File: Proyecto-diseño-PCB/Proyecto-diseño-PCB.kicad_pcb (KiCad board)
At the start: 4 copper layers, 41 parts, among them J1 USB_B_Micro, J2 PROGRAMACIÓN/DEPURACIÓN, J3 LADO A, J4 LADO B, SW1 BOTON, SW2 BOTON, SW3 RESET, U1 TPD2EUSB30, U2 LP2950-3.3_TO252, U3 PIC18LF45K50-I/P

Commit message: rest of the f-ing owl
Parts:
- C1, C2, C3: footprint Capacitor_THT:C_Disc_D3.4mm_W2.1mm_P2.50mm -> Capacitor_SMD:C_1206_3216Metric_Pad1.33x1.80mm_HandSolder
- C4, C5, C6, C7, C8: footprint Capacitor_THT:C_Disc_D3.4mm_W2.1mm_P2.50mm -> Capacitor_SMD:C_1206_3216Metric_Pad1.33x1.80mm_HandSolder; moved to B.Cu
- J3: footprint Connector_PinSocket_2.54mm:PinSocket_1x15_P2.54mm_Vertical -> Connector_PinSocket_2.54mm:PinSocket_1x16_P2.54mm_Vertical
- J4: footprint Connector_PinSocket_2.54mm:PinSocket_1x16_P2.54mm_Vertical -> Connector_PinSocket_2.54mm:PinSocket_1x14_P2.54mm_Vertical
- R1, R3: footprint Resistor_THT:R_Axial_DIN0204_L3.6mm_D1.6mm_P5.08mm_Horizontal -> Resistor_SMD:R_1206_3216Metric_Pad1.30x1.75mm_HandSolder; moved to B.Cu
- R10, R11, R12, R13, R2, R4, R5, R6, R7, R8, R9: footprint Resistor_THT:R_Axial_DIN0204_L3.6mm_D1.6mm_P5.08mm_Horizontal -> Resistor_SMD:R_1206_3216Metric_Pad1.30x1.75mm_HandSolder
- U1: moved to B.Cu
- moved R12 239.8 mm to (181.2, 73.7), turned to -90 degrees
- moved D5 237.8 mm to (169.8, 67.8)
- moved R11 235.6 mm to (177.9, 73.7), turned to -90 degrees
- moved D4 231.4 mm to (164.7, 67.8)
- moved R7 230.8 mm to (180.4, 83.6), turned to 180 degrees
- moved R5 227.9 mm to (180.5, 89.2), turned to 180 degrees
- moved R3 224.2 mm to (175.7, 78.7)
- moved R1 222.1 mm to (175.7, 81.7)
- moved C2 214.2 mm to (180.4, 86.4)
- moved R4 212.9 mm to (166.5, 92.3), turned to 90 degrees
- moved U1 207.1 mm to (171.3, 80.2), turned to 90 degrees
- moved R6 206.2 mm to (158.1, 92.3), turned to 90 degrees
- moved C8 205.6 mm to (167.3, 91.9), turned to 90 degrees
- moved D1 196.8 mm to (176.9, 88.4), turned to 90 degrees
- moved C1 194.4 mm to (162.2, 92.4), turned to -90 degrees
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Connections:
- net Net-(FL1-CB) renamed /VI
- J3 pad 10: /RA5 -> /RE0
- J3 pad 11: /RA4 -> /RA5
- J3 pad 12: /RA3 -> /RA4
- J3 pad 13: /RA2 -> /RA3
- J3 pad 14: /RA1 -> /RA2
- J3 pad 15: /RA0 -> /RA1
- U3 pad 19: /LED_ROJO -> /BOTON1
- U3 pad 20: /LED_VERDE -> /BOTON2
- U3 pad 21: /BOTON2 -> /LED_VERDE
- U3 pad 22: /BOTON1 -> /LED_ROJO
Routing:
- net 5V: track 0.00 -> 52.5 mm, vias 0 -> 2
- net /MASA_FUENTE: track 0.00 -> 43.8 mm
- net Net-(R4-Pad1): track 0.00 -> 20.1 mm
- net /MCLR: track 0.00 -> 17.9 mm
- net Net-(R5-Pad1): track 0.00 -> 15.7 mm
- net Net-(D4-K): track 0.00 -> 15.0 mm
- net /D+: track 0.00 -> 14.8 mm, vias 0 -> 1
- net /D-: track 0.00 -> 13.9 mm, vias 0 -> 1
- net Net-(D5-K): track 0.00 -> 13.2 mm
- net /PGD: track 0.00 -> 12.5 mm, vias 0 -> 1
- net /RC1: track 0.00 -> 12.3 mm
- net /RC0: track 0.00 -> 12.3 mm
- net /RC2: track 0.00 -> 12.3 mm
- net /RA7: track 0.00 -> 12.3 mm
- net /RA6: track 0.00 -> 12.3 mm
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- added copper zone on In1.Cu, net GND
- added copper zone on In2.Cu, net VDD
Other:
- board outline added: 76 x 35 mm

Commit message: estaba haciendo pruebas de las herramientas de kicad
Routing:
- net Net-(D4-K): track 15.0 -> 16.8 mm
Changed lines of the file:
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@@
 		(tags "Diode SOD523")
 		(property "Reference" "D7"
-			(at 2.032 -0.026 90)
+			(at 1.905 -0.026 180)
 			(layer "F.SilkS")
 			(effects
@@
 			(size 1.8 1.8)
 			(drill 0.9)
-			(layers "F&B.Cu" "*.Mask")
+			(layers "*.Cu" "*.Mask")
 			(remove_unused_layers no)
 			(net 7 "Net-(D4-K)")
@@
 			(size 1.8 1.8)
 			(drill 0.9)
-			(layers "F&B.Cu" "*.Mask")
+			(layers "*.Cu" "*.Mask")
 			(remove_unused_layers no)
 			(net 8 "/LED_ROJO")
@@
 		(tags "Diode SOD523")
 		(property "Reference" "D8"
-			(at 1.651 -0.127 180)
+			(at 1.778 0 180)
 			(layer "F.SilkS")
 			(effects
@@
 		(tags "capacitor handsolder")
 		(property "Reference" "C6"
-			(at 0 1.85 180)
+			(at -3.4675 -0.127 180)
 			(layer "B.SilkS")
 			(effects
@@
 		(tags "capacitor handsolder")
 		(property "Reference" "C4"
-			(at 3.6935 0 180)
+			(at -3.5455 0 180)
 			(layer "B.SilkS")
 			(effects
@@
 		(tags "capacitor handsolder")
 		(property "Reference" "C8"
-			(at -0.127 1.778 90)
+			(at 0 -2.032 90)
 			(layer "B.SilkS")
 			(effects
@@
 		(tags "DPAK TO-252 DPAK-3 TO-252-3 SOT-428")
 		(property "Reference" "U2"
-			(at 0 4.5 0)
+			(at 5.842 -0.0545 0)
 			(layer "B.SilkS")
 			(effects
@@
 		(tags "capacitor handsolder")
 		(property "Reference" "C5"
-			(at -3.732 0 0)
+			(at 3.761 0 0)
 			(layer "B.SilkS")
 			(effects
@@
 		(tags "Micro B USB SMD")
 		(property "Reference" "J1"
-			(at 0 3.3 90)
+			(at 6.216 -0.6 90)
 			(layer "B.SilkS")
 			(effects
@@
 	)
 	(segment
+		(start 164.719 67.818)
+		(end 164.719 69.596)
+		(width 0.17)
+		(layer "In2.Cu")
+		(net 7)
+	)
+	(segment
 		(start 167.259 70.358)
 		(end 169.799 72.898)
@@
 	)
 	(segment
-		(start 169.799 67.818)
-		(end 172.339 70.358)
+		(start 180.433 72.102)
+		(end 181.229 72.102)
 		(width 0.17)
 		(layer "F.Cu")
@@
 	)
 	(segment
-		(start 179.485 70.358)
-		(end 181.229 72.102)
+		(start 172.339 70.358)
+		(end 178.689 70.358)
 		(width 0.17)
 		(layer "F.Cu")
@@
 	)
 	(segment
-		(start 172.339 70.358)
-		(end 179.485 70.358)
+		(start 169.799 67.818)
+		(end 172.339 70.358)
+		(width 0.17)
+		(layer "F.Cu")
+		(net 10)
+	)
+	(segment
+		(start 178.689 70.358)
+		(end 180.433 72.102)
 		(width 0.17)
 		(layer "F.Cu")

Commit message: Entrega PCB 1
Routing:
- net Net-(D4-K): track 16.8 -> 15.0 mm
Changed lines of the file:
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@@
 	(generator_version "9.0")
 	(general
-		(thickness 1.6)
+		(thickness 1.684)
 		(legacy_teardrops no)
 	)
@@
 			(layer "dielectric 1"
 				(type "prepreg")
-				(thickness 0.1)
+				(thickness 0.127)
 				(material "FR4")
 				(epsilon_r 4.5)
@@
 			(layer "dielectric 2"
 				(type "core")
-				(thickness 1.24)
+				(thickness 1.27)
 				(material "FR4")
 				(epsilon_r 4.5)
@@
 			(layer "dielectric 3"
 				(type "prepreg")
-				(thickness 0.1)
+				(thickness 0.127)
 				(material "FR4")
 				(epsilon_r 4.5)
@@
 		(grid_origin 164.719 98.298)
 		(pcbplotparams
-			(layerselection 0x00000000_00000000_55555555_5755f5ff)
-			(plot_on_all_layers_selection 0x00000000_00000000_00000000_00000000)
+			(layerselection 0x00000000_00000000_55555555_55555555)
+			(plot_on_all_layers_selection 0x00000000_00000000_00000002_22000000)
 			(disableapertmacros no)
 			(usegerberextensions no)
@@
 			(pdf_back_fp_property_popups yes)
 			(pdf_metadata yes)
-			(pdf_single_document no)
+			(pdf_single_document yes)
 			(dxfpolygonmode yes)
 			(dxfimperialunits yes)
@@
 			(psnegative no)
 			(psa4output no)
-			(plot_black_and_white yes)
+			(plot_black_and_white no)
 			(sketchpadsonfab no)
 			(plotpadnumbers no)
@@
 			(crossoutdnponfab yes)
 			(subtractmaskfromsilk no)
-			(outputformat 1)
-			(mirror no)
+			(outputformat 4)
+			(mirror yes)
 			(drillshape 1)
 			(scaleselection 1)
-			(outputdirectory "")
+			(outputdirectory "../Esquemático/")
 		)
 	)
@@
 		)
 		(property "Value" "10n"
-			(at 0 1.85 90)
+			(at -0.1725 1.542 270)
 			(layer "F.Fab")
 			(effects
@@
 		(tags "PIC18LF45K50-I/P ")
 		(property "Reference" "U3"
-			(at 7.62 24.13 90)
+			(at 8.636 24.13 0)
 			(unlocked yes)
 			(layer "F.SilkS")
@@
 		)
 		(property "Value" "PIC18LF45K50-I/P"
-			(at 7.62 24.13 90)
+			(at 6.35 24.13 0)
 			(unlocked yes)
 			(layer "F.Fab")
@@
 			(layer "F.Fab")
 		)
-		(fp_text user "*"
-			(at 0 -1.5113 90)
-			(unlocked yes)
-			(layer "F.SilkS")
-			(effects
-				(font
-					(size 1 1)
-					(thickness 0.15)
-				)
-			)
-		)
-		(fp_text user "*"
-			(at 0 -1.5113 90)
-			(layer "F.SilkS")
-			(effects
-				(font
-					(size 1 1)
-					(thickness 0.15)
-				)
-			)
-		)
-		(fp_text user "*"
-			(at 0.508 0 90)
-			(layer "F.Fab")
-			(effects
-				(font
-					(size 1 1)
-					(thickness 0.15)
-				)
-			)
-		)
-		(fp_text user "${REFERENCE}"
-			(at 7.62 24.13 90)
-			(unlocked yes)
-			(layer "F.Fab")
-			(effects
-				(font
-					(size 1 1)
-					(thickness 0.15)
-				)
-			)
-		)
-		(fp_text user "*"
-			(at 0.508 0 90)
-			(unlocked yes)
-			(layer "F.Fab")
-			(effects
-				(font
-					(size 1 1)
-					(thickness 0.15)
-				)
-			)
-		)
 		(pad "1" thru_hole rect
 			(at 0 0 90)
@@
 		)
 		(property "Value" "RESET"
-			(at 2.25 5.38988 0)
+			(at 2.25 -1.524 0)
 			(layer "F.Fab")
 			(effects
@@
 			(at 3.75 6.7 90)
 			(layer "F.Fab")
+			(hide yes)
 			(effects
 				(font
@@
 		(tags "resistor handsolder")
 		(property "Reference" "R4"
-			(at -3.575 -0.018 90)
+			(at -3.448 -0.78 90)
 			(layer "F.SilkS")
 			(effects
@@
 		)
 		(property "Value" "100"
-			(at 0 1.83 90)
+			(at -3.194 0.236 270)
 			(layer "F.Fab")
 			(effects
@@
 		)
 		(property "Value" "100"
-			(at 0 1.83 0)
+			(at -2.54 -0.254 90)
 			(layer "F.Fab")
 			(effects
@@
 		)
 		(property "Value" "100"
-			(at 0 1.83 0)
+			(at -0.101 2.032 180)
 			(layer "F.Fab")
 			(effects
@@
 		(tags "Diode SOD523")
 		(property "Reference" "D7"
-			(at 1.905 -0.026 180)
+			(at 1.905 -0.026 0)
 			(layer "F.SilkS")
 			(effects
@@
 			(at 0 1.4 90)
 			(layer "F.Fab")
+			(hide yes)
 			(effects
 				(font
@@
 			(layer "F.Fab")
 		)
-		(fp_text user "${REFERENCE}"
-			(at 0 -1.3 90)
-			(layer "F.Fab")
-			(effects
-				(font
-					(size 1 1)
-					(thickness 0.15)
-				)
-			)
-		)
 		(pad "1" smd roundrect
 			(at -0.7 0 90)
@@
 		)
 		(property "Value" "10n"
-			(at 0 1.85 0)
+			(at 2.5785 -0.762 90)
 			(layer "F.Fab")
 			(effects
@@
 		)
 		(property "Value" "1K"
-			(at 0 1.83 90)
+			(at 0 -1.905 90)
 			(layer "F.Fab")
 			(effects
@@
 		)
 		(property "Value" "100n"
-			(at 0 1.85 0)
+			(at 4.064 0 0)
 			(layer "F.Fab")
 			(effects
@@
 			(at 3.75 6.7 90)
 			(layer "F.Fab")
+			(hide yes)
 			(effects
 				(font
@@
 		)
 		(property "Value" "1K"
-			(at 0 1.83 90)
+			(at 0 -1.778 90)
 			(layer "F.Fab")
 			(effects
@@
 			(at 1.27 2 0)
 			(layer "F.Fab")
+			(hide yes)
 			(effects
 				(font
@@
 			(at 0 1.4 90)
 			(layer "F.Fab")
+			(hide yes)
 			(effects
 				(font
@@
 			(layer "F.Fab")
 		)
-		(fp_text user "${REFERENCE}"
-			(at 0 -1.3 90)
-			(layer "F.Fab")
-			(effects
-				(font
-					(size 1 1)
-					(thickness 0.15)
-				)
-			)
-		)
 		(pad "1" smd roundrect
 			(at -0.7 0 270)
@@
 		)
 		(property "Value" "100"
-			(at 0 1.83 0)
+			(at 0.101 1.778 180)
 			(layer "F.Fab")
 			(effects
@@
 		)
 		(property "Value" "100"
-			(at 0 1.83 0)
+			(at -0.101 -1.778 180)
 			(layer "F.Fab")
 			(effects
@@
 			(at 0 35.79 270)
 			(layer "F.Fab")
+			(hide yes)
 			(effects
 				(font
@@
 		)
 		(property "Value" "100K"
-			(at 0 1.83 90)
+			(at -0.146 -1.796 270)
 			(layer "F.Fab")
-			(hide yes)
 			(effects
 				(font
@@
 			(at 0 1.4 90)
 			(layer "F.Fab")
+			(hide yes)
 			(effects
 				(font
@@
 			(layer "F.Fab")
 		)
-		(fp_text user "${REFERENCE}"
-			(at 0 -1.3 90)
-			(layer "F.Fab")
-			(effects
-				(font
-					(size 1 1)
-					(thickness 0.15)
-				)
-			)
-		)
 		(pad "1" smd roundrect
 			(at -0.7 0 270)
@@
 			(at 0 40.87 270)
 			(layer "F.Fab")
+			(hide yes)
 			(effects
 				(font
@@
 			(at 3.048 5.08 90)
 			(layer "F.Fab")
+			(hide yes)
 			(effects
 				(font
@@
 			(at 0 1.4 90)
 			(layer "F.Fab")
+			(hide yes)
 			(effects
 				(font
@@
 			(layer "F.Fab")
 		)
-		(fp_text user "${REFERENCE}"
-			(at 0 -1.3 90)
-			(layer "F.Fab")
-			(effects
-				(font
-					(size 1 1)
-					(thickness 0.15)
-				)
-			)
-		)
 		(pad "1" smd roundrect
 			(at -0.7 0 90)
@@
 			(at 0 1.4 90)
 			(layer "F.Fab")
+			(hide yes)
 			(effects
 				(font
@@
 			(layer "F.Fab")
 		)
-		(fp_text user "${REFERENCE}"
-			(at 0 -1.3 90)
-			(layer "F.Fab")
-			(effects
-				(font
-					(size 1 1)
-					(thickness 0.15)
-				)
-			)
-		)
 		(pad "1" smd roundrect
 			(at -0.7 0 270)
@@
 		)
 		(property "Value" "100n"
-			(at 0 -1.85 180)
+			(at -4.4835 0 180)
 			(layer "B.Fab")
 			(effects
@@
 		)
 		(property "Value" "1u"
-			(at 0 -1.85 180)
+			(at -3.4185 0 180)
 			(layer "B.Fab")
 			(effects
@@
 		)
 		(property "Value" "LP2950-3.3_TO252"
-			(at 0 -4.5 0)
+			(at 12.192 -2.4675 0)
 			(layer "B.Fab")
+			(hide yes)
 			(effects
 				(font
@@
 		)
 		(property "Value" "2.2u"
-			(at 0 -1.85 0)
+			(at 4.396 0 0)
 			(layer "B.Fab")
 			(effects
@@
 			(at 0 -1.5 90)
 			(layer "B.Fab")
+			(hide yes)
 			(effects
 				(font
@@
 		)
 		(fp_text user "${REFERENCE}"
-			(at 0 1.5 90)
+			(at -1.825 0.057 0)
 			(layer "B.Fab")
 			(effects
@@
 		)
 		(property "Value" "100"
-			(at 0 -1.83 0)
+			(at 0 1.825 0)
 			(layer "B.Fab")
 			(effects
@@
 		)
 		(property "Value" "BNX025"
-			(at -1.9 -7.75 0)
+			(at 0 -1.778 0)
 			(layer "B.Fab")
 			(effects
@@
 		)
 		(fp_text user "${REFERENCE}"
-			(at 10.865 0 0)
+			(at 0.254 0 0)
 			(layer "B.Fab")
 			(effects
@@
 			(at 0 -4.6 90)
 			(layer "B.Fab")
+			(hide yes)
 			(effects
 				(font
@@
 		(net 7)
 	)
-	(segment
-		(start 164.719 67.818)
-		(end 164.719 69.596)
-		(width 0.17)
-		(layer "In2.Cu")
-		(net 7)
-	)

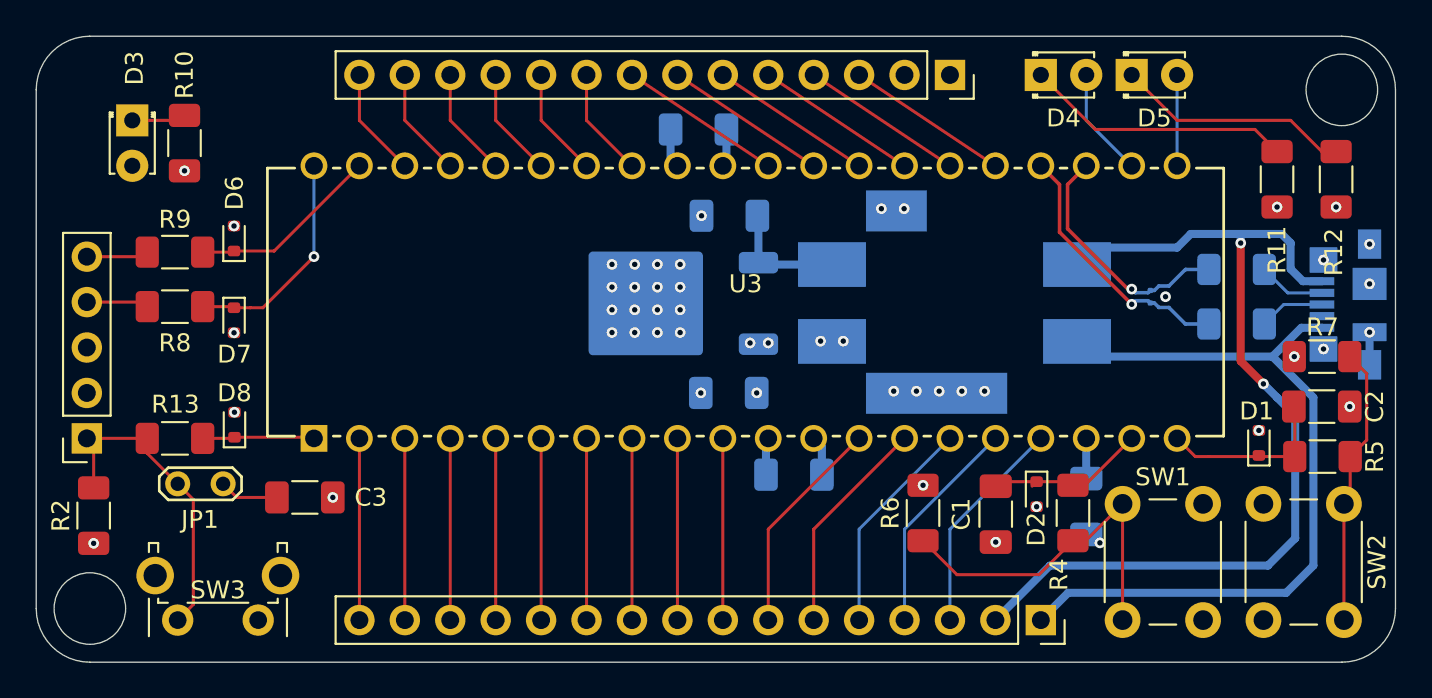
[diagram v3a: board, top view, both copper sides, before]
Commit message: Modifiqué tamaño de pistas
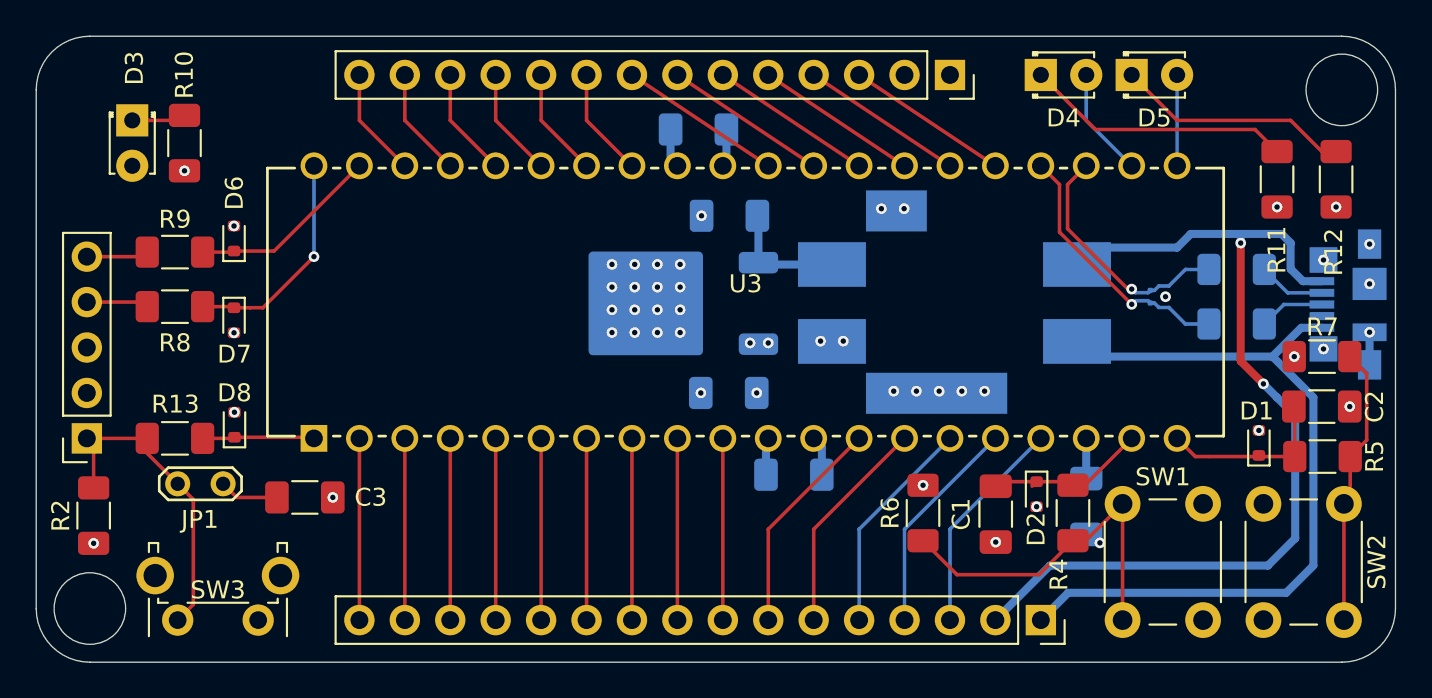
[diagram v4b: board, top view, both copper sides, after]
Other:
- board text added: "PCB Way: https://www.pcbway.com/capabilities.html Tamaño min pista: 4mil (6mil recomendado) Separación min: 4mil (6mil recomendado) Vias - agujeros: 0.2mm - 6.2mm Vias - anillo min: 0.15mm"

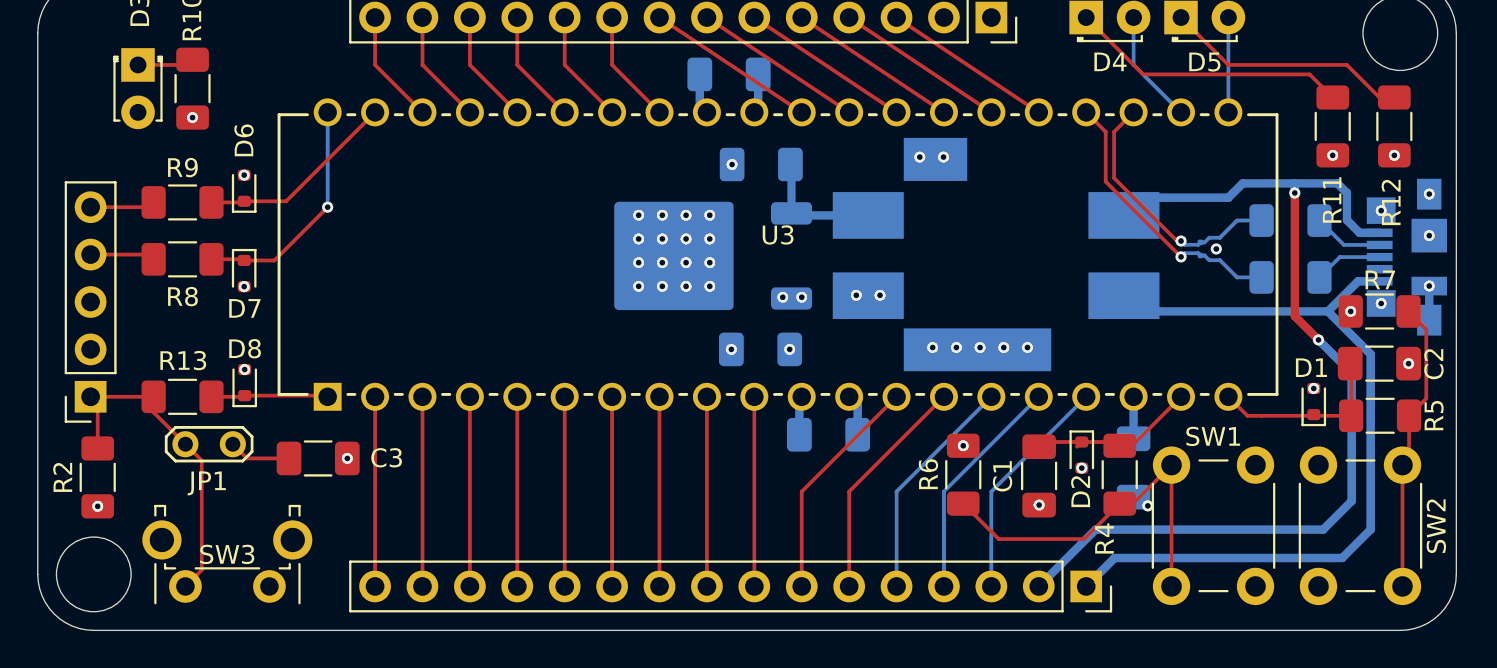
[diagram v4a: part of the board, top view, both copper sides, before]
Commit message: Correccion: vias separadas de pads
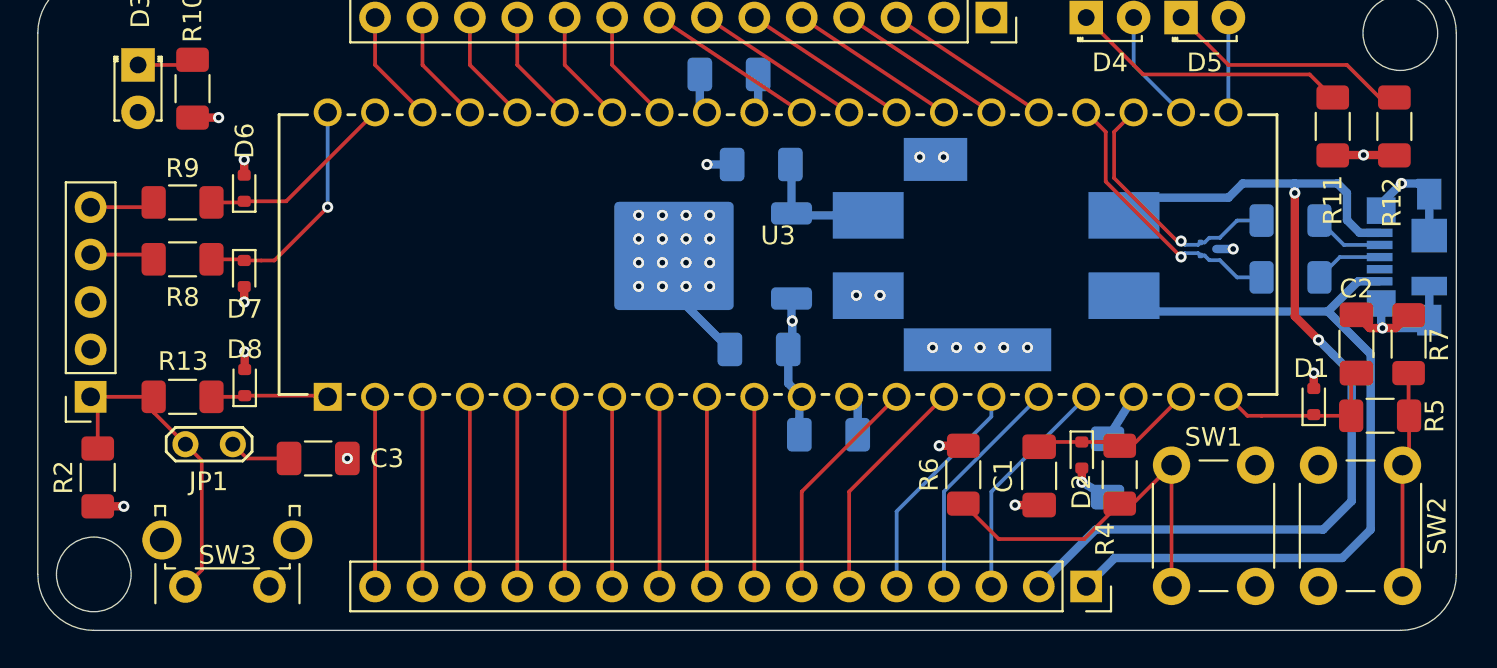
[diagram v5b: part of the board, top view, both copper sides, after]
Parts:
- moved R7 2.34 mm to (182.0, 85.3), turned to 90 degrees
- moved C2 1.62 mm to (179.2, 85.3), turned to 90 degrees
- moved C8 1.40 mm to (165.9, 91.9)
- moved C5 0.08 mm to (147.2, 85.6)
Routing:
- net GND: track 6.16 -> 41.0 mm, vias 47 -> 39
- net VDD: track 7.23 -> 14.9 mm, vias 4 -> 2
- net Net-(R5-Pad1): track 15.7 -> 11.6 mm
